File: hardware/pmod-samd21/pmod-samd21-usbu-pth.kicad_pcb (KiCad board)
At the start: 2 copper layers, 18.2 x 29 mm, 19 parts, among them J1 PMOD-2x6-MALE, J2 PMOD-2x6-FEMALE, J3 USB_B_Micro, Q1 2N7002PW, U1 ATSAMD21G-A, Y1 32.768kHz

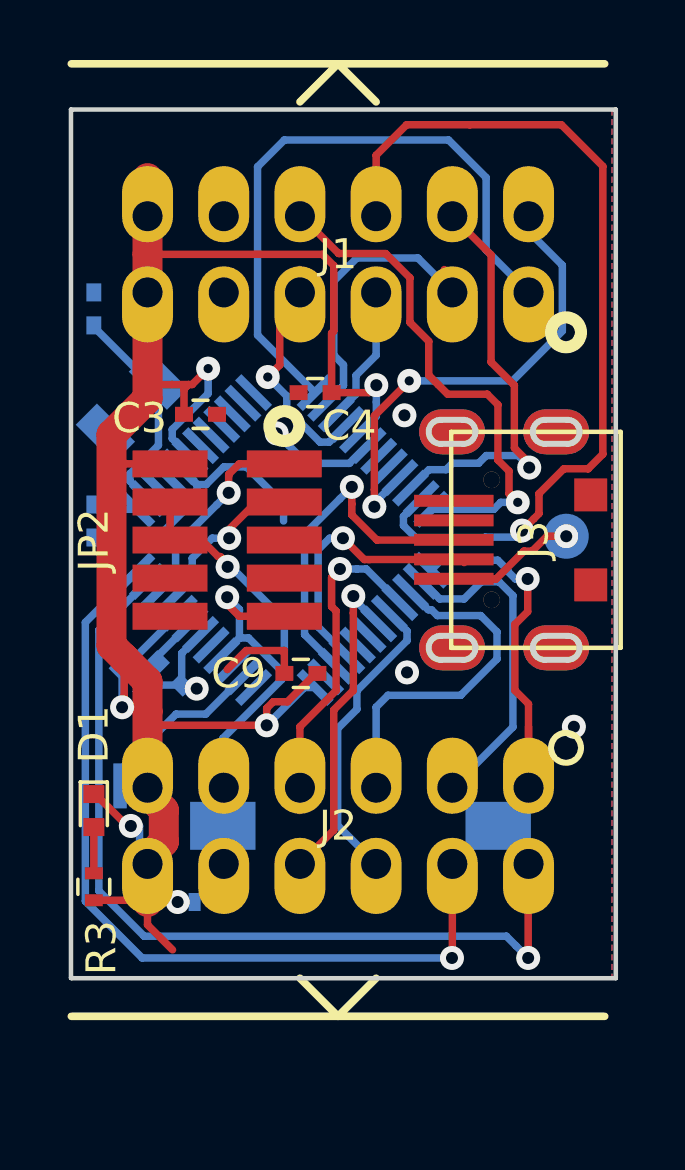
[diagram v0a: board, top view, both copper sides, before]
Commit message: pmod-samd21 : routed and ready for fab
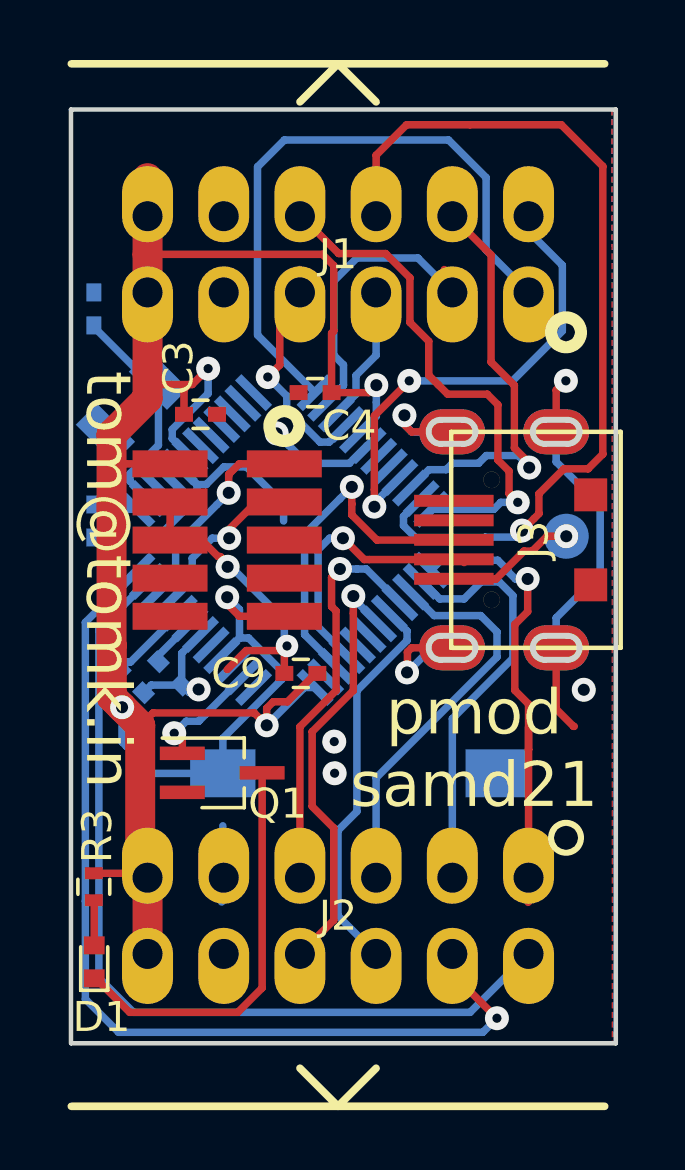
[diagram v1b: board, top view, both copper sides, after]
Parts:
- Q1: moved to F.Cu
- moved R1 5.21 mm to (145.1, 156.6), turned to 90 degrees
- moved D1 5.04 mm to (143.5, 163.3), turned to 90 degrees
- moved Q1 3.27 mm to (147.8, 157.0), turned to 0 degrees
- moved J2 3.00 mm to (151.7, 161.8)
- moved S1 1.75 mm to (152.4, 157.0)
- turned R3 to 90 degrees
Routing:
- net GND: track 26.7 -> 50.5 mm, vias 6 -> 10
- net Net-(D1-Pad1): track 3.30 -> 13.6 mm, vias 1 -> 0
- net /SER5_1: track 26.6 -> 32.1 mm
- net /SER1_0: track 10.5 -> 14.8 mm
- net /SER1_1: track 11.0 -> 14.0 mm
- net /SER5_2: track 10.1 -> 13.1 mm
- net /SER5_3: track 11.6 -> 14.5 mm
- net /SER1_3: track 11.1 -> 13.4 mm
- net /BLUE_LED: track 5.91 -> 3.85 mm, vias 0 -> 1
- net /SER5_0: track 28.1 -> 30.1 mm, vias 1 -> 0
- net /~RESET: track 15.1 -> 13.4 mm
- net /SER1_2: track 11.7 -> 13.3 mm
- net +3V3: track 71.9 -> 70.5 mm, vias 5 -> 4
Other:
- board size 18.2 x 29 mm -> 18.2 x 31.1 mm
- board text added: "Jan 2019"
- board text added: "pmod samd21"
- board text removed: "Dec 2018"
- board text removed: "pmod-samd21"
